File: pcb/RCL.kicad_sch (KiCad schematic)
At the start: 86 parts, among them J1 USB_C_Receptacle, J2 Conn_01x02_Pin, J3 Conn_01x05_Pin, Q1 BSP613, Q2 AO3416A, Q3 AO3416A, Q4 AO3416A, SW1 SW_SPDT, SW2 SW_DIP_x02, SW3 SW_Push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

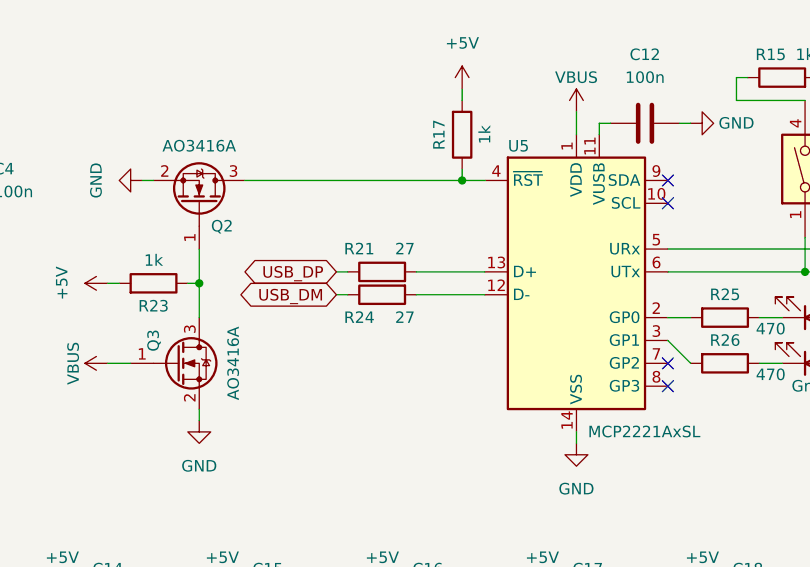
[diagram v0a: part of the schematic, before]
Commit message: Add dimensioning
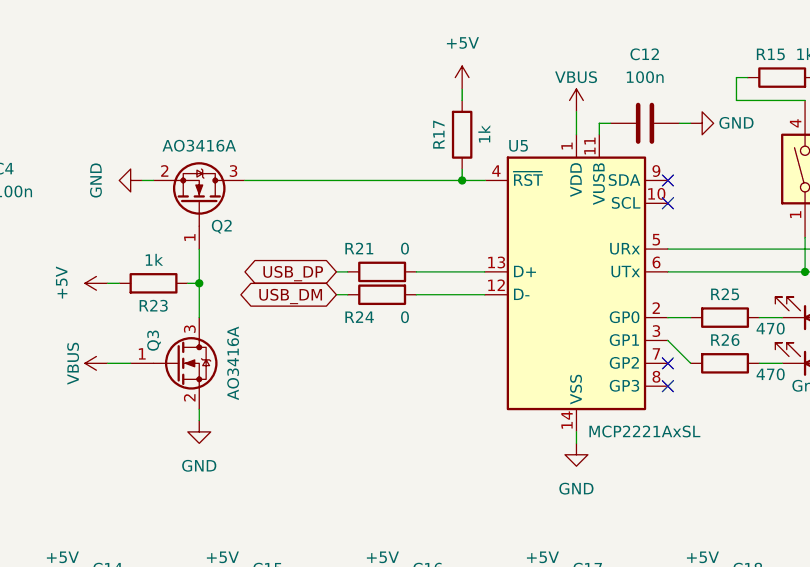
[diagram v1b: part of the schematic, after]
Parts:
- R21, R24: value 27 -> 0; Vendor HTL -> (none); VendorId 102920 -> (none)
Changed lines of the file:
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@@
       (effects (font (size 1.27 1.27)))
     )
-    (property "Value" "27" (at 85.09 120.65 90)
+    (property "Value" "0" (at 85.09 120.65 90)
       (effects (font (size 1.27 1.27)))
     )
@@
       (effects (font (size 1.27 1.27)) hide)
     )
-    (property "Vendor" "HTL" (at 82.55 118.11 0)
-      (effects (font (size 1.27 1.27)) hide)
-    )
-    (property "VendorId" "102920" (at 82.55 118.11 0)
+    (property "Vendor" "" (at 82.55 118.11 0)
+      (effects (font (size 1.27 1.27)) hide)
+    )
+    (property "VendorId" "" (at 82.55 118.11 0)
       (effects (font (size 1.27 1.27)) hide)
     )
@@
       (effects (font (size 1.27 1.27)))
     )
-    (property "Value" "27" (at 85.09 113.03 90)
+    (property "Value" "0" (at 85.09 113.03 90)
       (effects (font (size 1.27 1.27)))
     )
@@
       (effects (font (size 1.27 1.27)) hide)
     )
-    (property "Vendor" "HTL" (at 82.55 115.57 0)
-      (effects (font (size 1.27 1.27)) hide)
-    )
-    (property "VendorId" "102920" (at 82.55 115.57 0)
-      (effects (font (size 1.27 1.27)) hide)
-    )
+    (property "Vendor" "" (at 82.55 115.57 0)
+      (effects (font (size 1.27 1.27)) hide)
+    )
+    (property "VendorId" "" (at 82.55 115.57 0)
+      (effects (font (size 1.27 1.27)) hide)
+    )

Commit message: Add missing vendor(id)
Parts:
- D10, D11, D12, D13, D14, D15, D16, D17: Vendor (none) -> HTL; VendorId (none) -> 103607
- J3: Vendor (none) -> HTL; VendorId (none) -> 101546
- R21, R24: Vendor (none) -> DigiKey; VendorId (none) -> RMCF0603ZT0R00CT-ND
- U5: Vendor (none) -> DigiKey; VendorId (none) -> 150-MCP2221AT-I/SLCT-ND
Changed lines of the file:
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@@
       (effects (font (size 1.27 1.27)) (justify left top) hide)
+    )
+    (property "Vendor" "HTL" (at 29.21 161.29 0)
+      (effects (font (size 1.27 1.27)) hide)
+    )
+    (property "VendorId" "103607" (at 29.21 161.29 0)
+      (effects (font (size 1.27 1.27)) hide)
     )
     (pin "6")
@@
     (property "Datasheet" "http://www.led-color.com/upload/201506/APA102%20LED.pdf" (at 97.79 170.815 0)
       (effects (font (size 1.27 1.27)) (justify left top) hide)
+    )
+    (property "Vendor" "HTL" (at 100.33 161.29 0)
+      (effects (font (size 1.27 1.27)) hide)
+    )
+    (property "VendorId" "103607" (at 100.33 161.29 0)
+      (effects (font (size 1.27 1.27)) hide)
     )
     (pin "6")
@@
     )
     (property "Datasheet" "http://ww1.microchip.com/downloads/en/DeviceDoc/20005565B.pdf" (at 104.14 100.33 0)
+      (effects (font (size 1.27 1.27)) hide)
+    )
+    (property "Vendor" "DigiKey" (at 104.14 118.11 0)
+      (effects (font (size 1.27 1.27)) hide)
+    )
+    (property "VendorId" "150-MCP2221AT-I/SLCT-ND" (at 104.14 118.11 0)
       (effects (font (size 1.27 1.27)) hide)
     )
@@
       (effects (font (size 1.27 1.27)) (justify left top) hide)
     )
+    (property "Vendor" "HTL" (at 46.99 161.29 0)
+      (effects (font (size 1.27 1.27)) hide)
+    )
+    (property "VendorId" "103607" (at 46.99 161.29 0)
+      (effects (font (size 1.27 1.27)) hide)
+    )
     (pin "6")
     (pin "1")
@@
       (effects (font (size 1.27 1.27)) hide)
     )
+    (property "Vendor" "HTL" (at 255.27 129.54 0)
+      (effects (font (size 1.27 1.27)) hide)
+    )
+    (property "VendorId" "101546" (at 255.27 129.54 0)
+      (effects (font (size 1.27 1.27)) hide)
+    )
     (pin "4")
     (pin "5")
@@
       (effects (font (size 1.27 1.27)) (justify left top) hide)
     )
+    (property "Vendor" "HTL" (at 82.55 161.29 0)
+      (effects (font (size 1.27 1.27)) hide)
+    )
+    (property "VendorId" "103607" (at 82.55 161.29 0)
+      (effects (font (size 1.27 1.27)) hide)
+    )
     (pin "6")
     (pin "1")
@@
       (effects (font (size 1.27 1.27)) (justify left top) hide)
     )
+    (property "Vendor" "HTL" (at 153.67 161.29 0)
+      (effects (font (size 1.27 1.27)) hide)
+    )
+    (property "VendorId" "103607" (at 153.67 161.29 0)
+      (effects (font (size 1.27 1.27)) hide)
+    )
     (pin "6")
     (pin "1")
@@
       (effects (font (size 1.27 1.27)) (justify left top) hide)
     )
+    (property "Vendor" "HTL" (at 118.11 161.29 0)
+      (effects (font (size 1.27 1.27)) hide)
+    )
+    (property "VendorId" "103607" (at 118.11 161.29 0)
+      (effects (font (size 1.27 1.27)) hide)
+    )
     (pin "6")
     (pin "1")
@@
       (effects (font (size 1.27 1.27)) hide)
     )
-    (property "Vendor" "" (at 82.55 118.11 0)
-      (effects (font (size 1.27 1.27)) hide)
-    )
-    (property "VendorId" "" (at 82.55 118.11 0)
+    (property "Vendor" "DigiKey" (at 82.55 118.11 0)
+      (effects (font (size 1.27 1.27)) hide)
+    )
+    (property "VendorId" "RMCF0603ZT0R00CT-ND" (at 82.55 118.11 0)
       (effects (font (size 1.27 1.27)) hide)
     )
@@
       (effects (font (size 1.27 1.27)) hide)
     )
-    (property "Vendor" "" (at 82.55 115.57 0)
-      (effects (font (size 1.27 1.27)) hide)
-    )
-    (property "VendorId" "" (at 82.55 115.57 0)
+    (property "Vendor" "DigiKey" (at 82.55 115.57 0)
+      (effects (font (size 1.27 1.27)) hide)
+    )
+    (property "VendorId" "RMCF0603ZT0R00CT-ND" (at 82.55 115.57 0)
       (effects (font (size 1.27 1.27)) hide)
     )
@@
       (effects (font (size 1.27 1.27)) (justify left top) hide)
     )
+    (property "Vendor" "HTL" (at 64.77 161.29 0)
+      (effects (font (size 1.27 1.27)) hide)
+    )
+    (property "VendorId" "103607" (at 64.77 161.29 0)
+      (effects (font (size 1.27 1.27)) hide)
+    )
     (pin "6")
     (pin "1")
@@
       (effects (font (size 1.27 1.27)) (justify left top) hide)
     )
+    (property "Vendor" "HTL" (at 135.89 161.29 0)
+      (effects (font (size 1.27 1.27)) hide)
+    )
+    (property "VendorId" "103607" (at 135.89 161.29 0)
+      (effects (font (size 1.27 1.27)) hide)
+    )
     (pin "6")

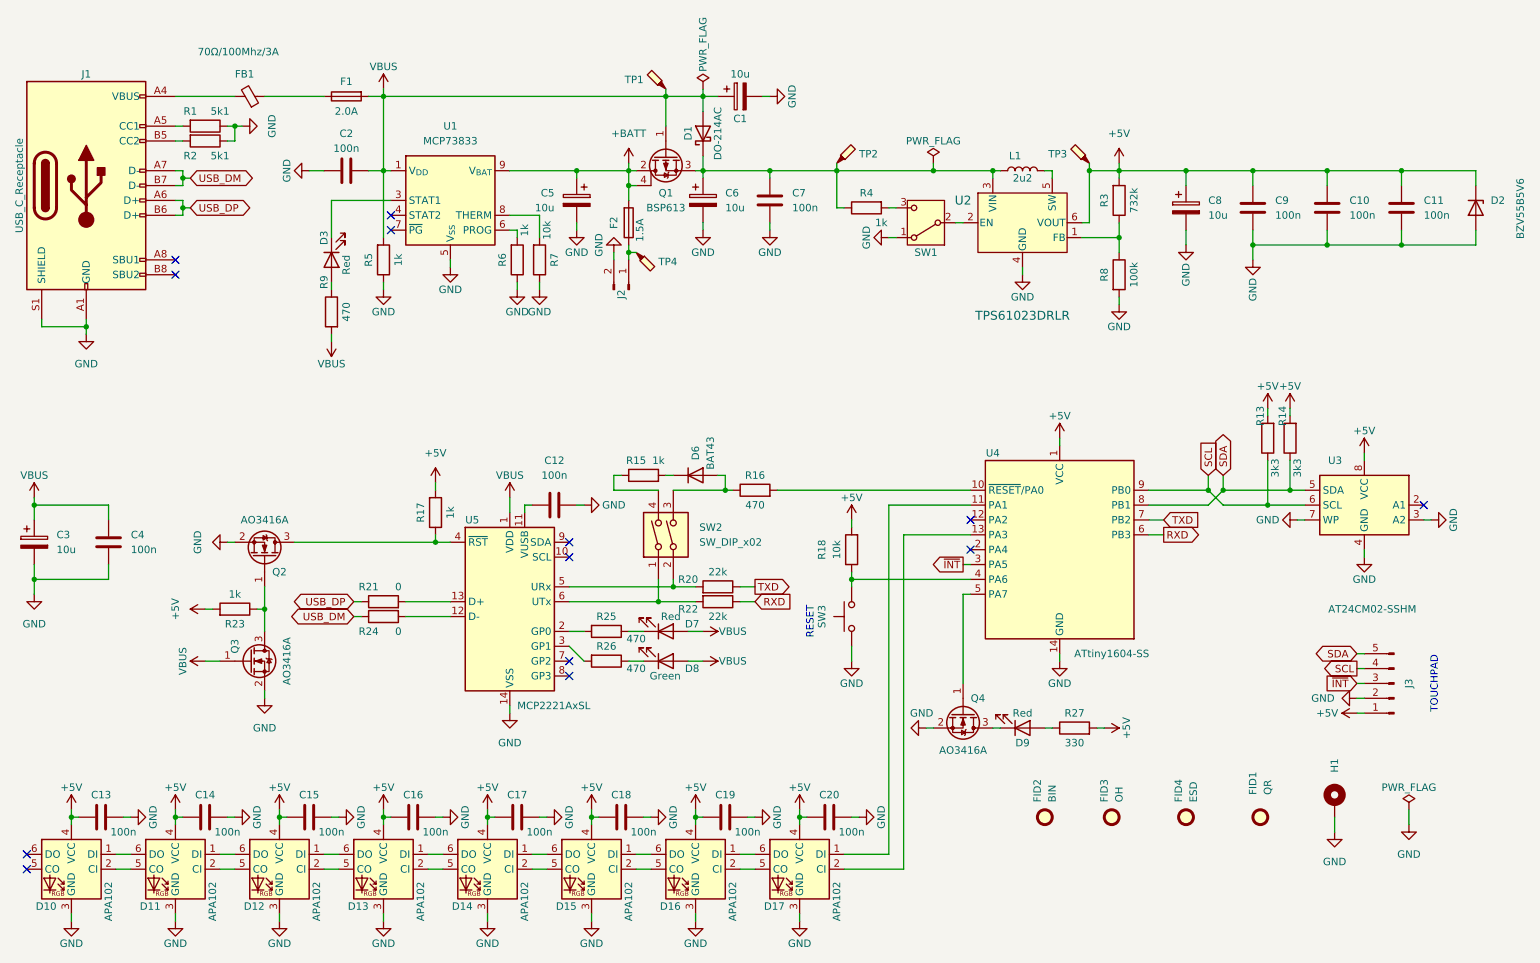
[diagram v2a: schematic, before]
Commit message: Increase KiCAD version
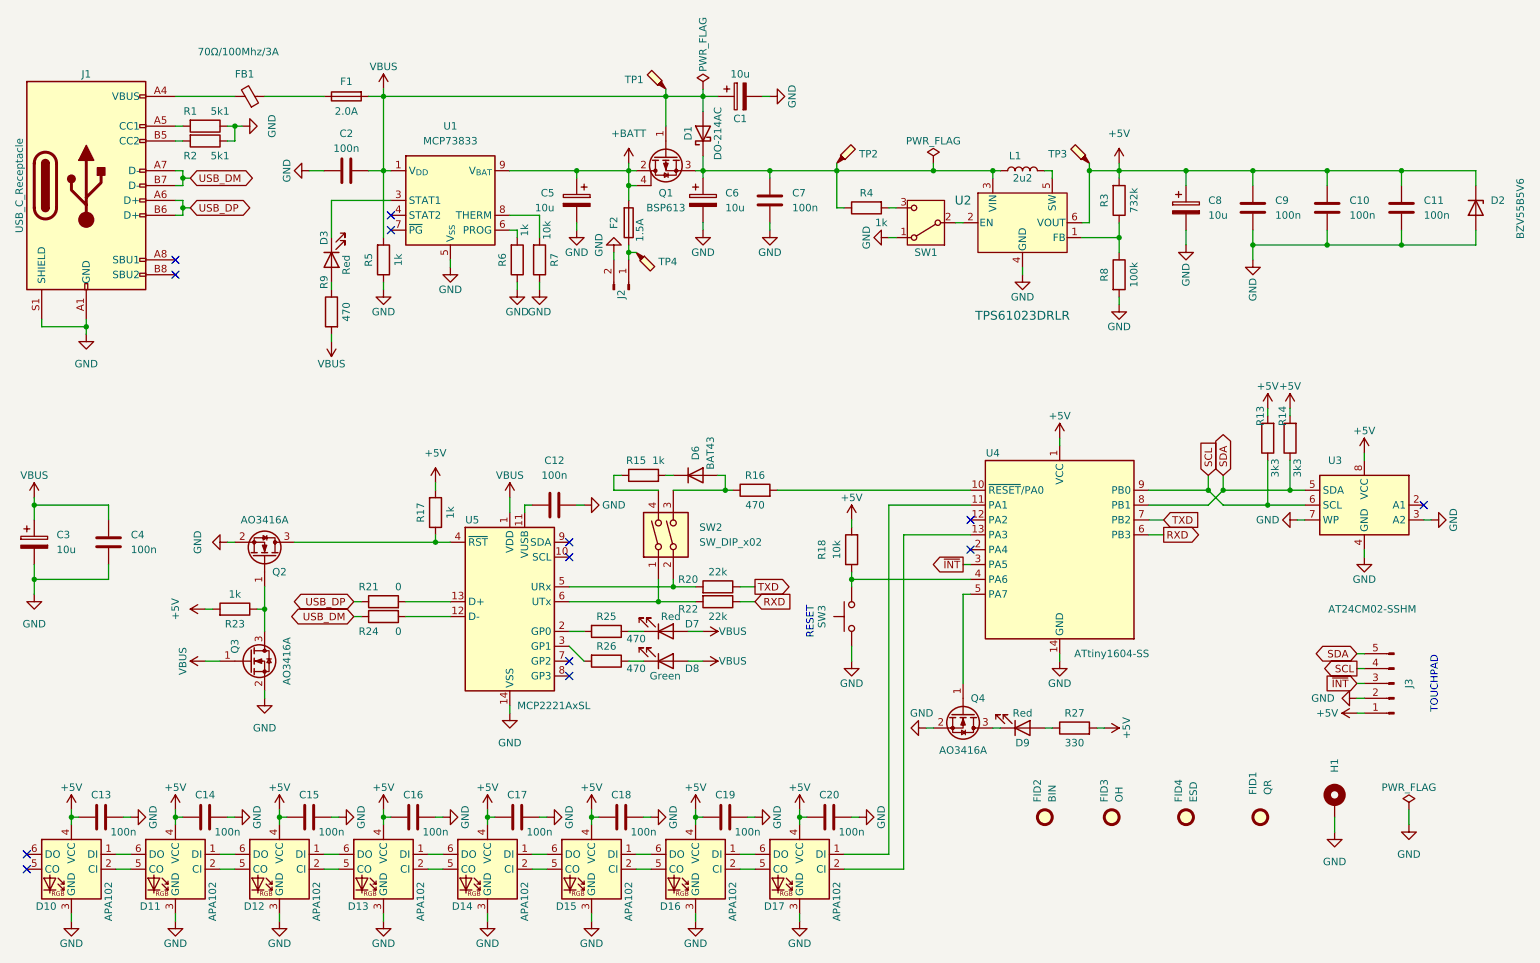
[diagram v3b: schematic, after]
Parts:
- Q1: symbol Device:Q_PMOS_GDSD -> Transistor_FET:Q_PMOS_GDSD
